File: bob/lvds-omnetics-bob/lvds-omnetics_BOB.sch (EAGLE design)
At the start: 31 parts, among them U1 SN65LVDS1, U2 SN65LVDS2, U3 SN65LVDS1, U4 SN65LVDS2, U5 SN65LVDS1, U6 SN65LVDS1

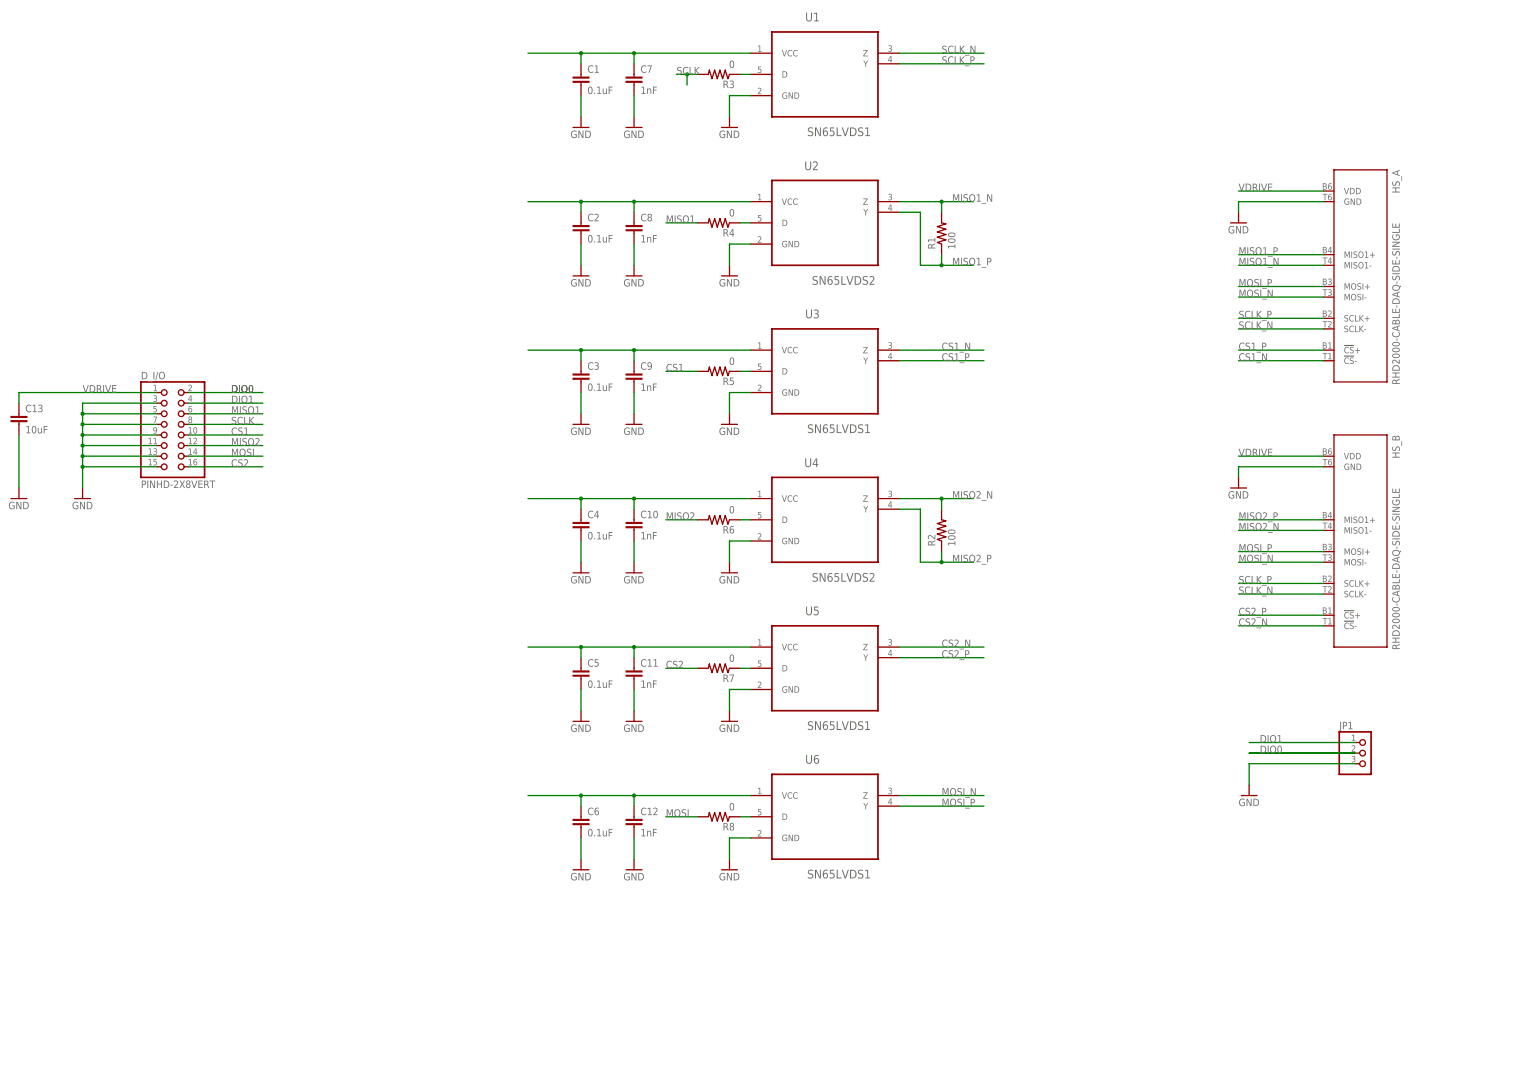
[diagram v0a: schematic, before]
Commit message: Fixed logo and made a part in the puggleboard library so that it is easy to add. Many minor changes to both boards. Should be just about ready to go.
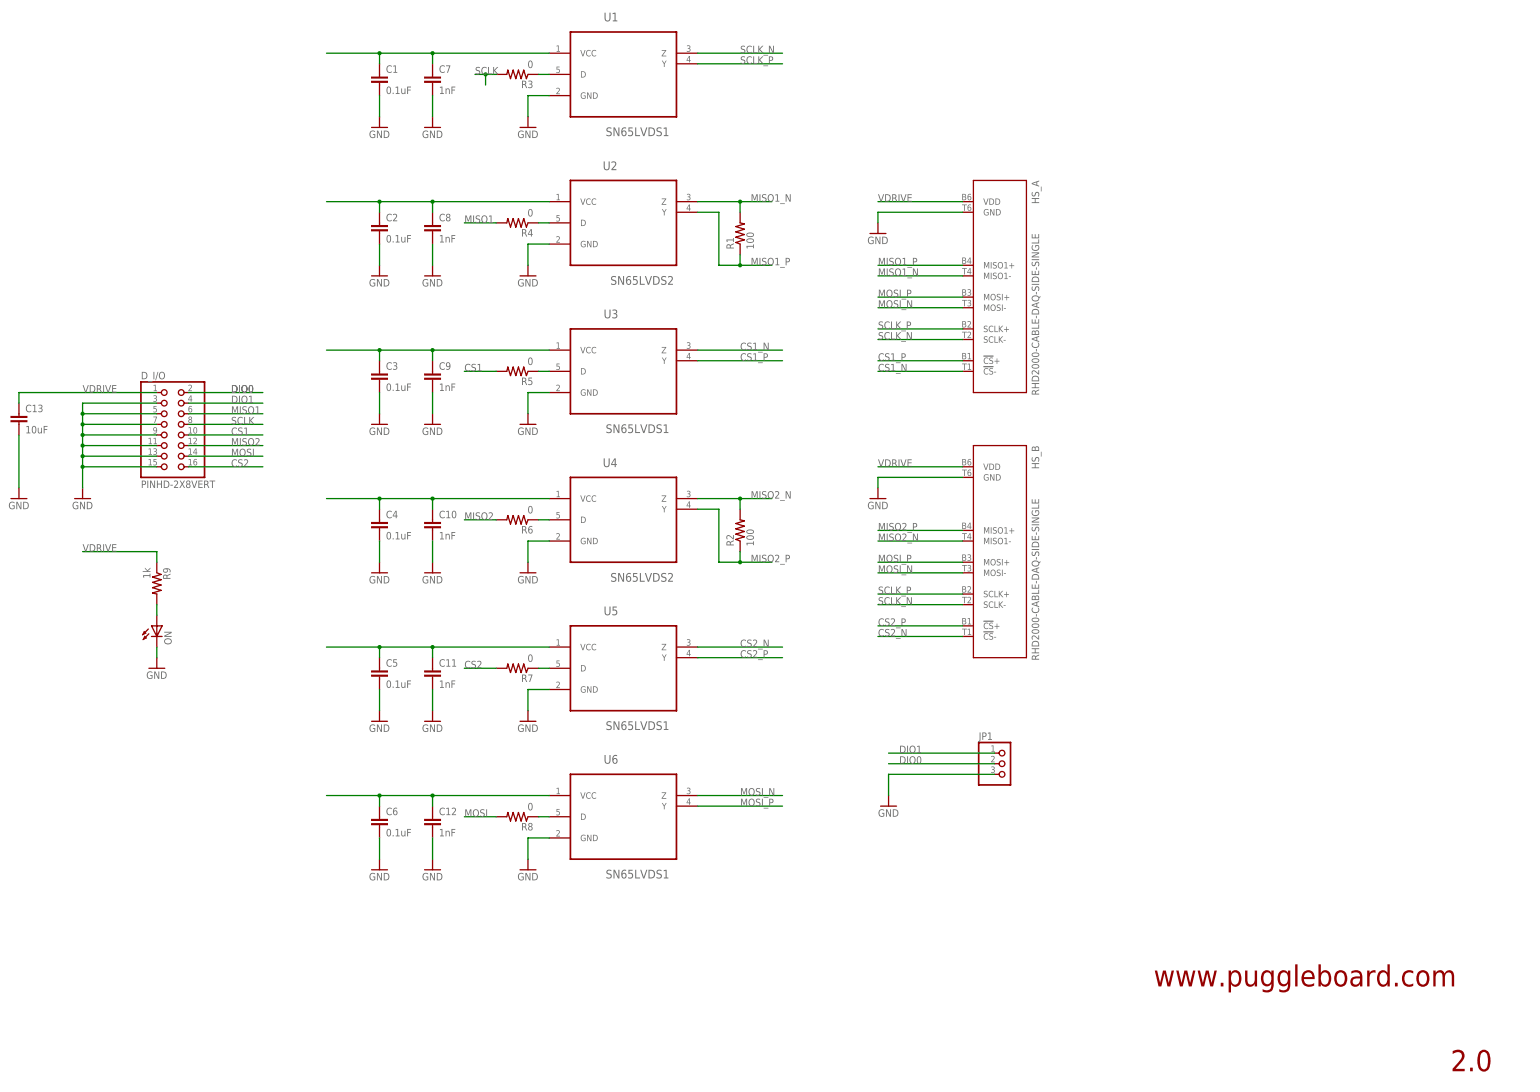
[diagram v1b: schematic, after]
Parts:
- added ON: LED-CHIP0805, puggleboard:LED-CHIP0805
- added R9: 1k, puggleboard:R_0603
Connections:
- new net N$9: ON.A, R9.2
- net GND: now also ON.C
- net VDRIVE: now also R9.1
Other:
- note added: "2.0"
- note added: "www.puggleboard.com"
- moved on the sheet: C1, C10, C11, C12, C2, C3, C4, C5, C6, C7, C8, C9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

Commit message: Many final changes to design before fabrication.
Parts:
- C1: value 0.1uF -> 10uF; device puggleboard:C_0603 -> puggleboard:C_0805
- C13: value 10uF -> 1nF; device puggleboard:C_0805 -> puggleboard:C_0603
- C7: value 1nF -> 0.1uF
- R1: value 100 -> 1k
- R2: value 100 -> 0
- R8: value 0 -> 100
- R9: value 1k -> 100
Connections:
- removed net VDRIVE: C1.1, C10.1, C11.1, C12.1, C13.1, C2.1, C3.1, C4.1, C5.1, C6.1, C7.1, C8.1, C9.1, D_I/O.1, HS_A.VDD, HS_B.VDD, R9.1, U1.VCC, U2.VCC, U3.VCC, U4.VCC, U5.VCC, U6.VCC
- new net VCC: C1.1, C10.1, C11.1, C12.1, C13.1, C2.1, C3.1, C4.1, C5.1, C6.1, C7.1, C8.1, C9.1, D_I/O.1, HS_A.VDD, HS_B.VDD, R1.1, U1.VCC, U2.VCC, U3.VCC, U4.VCC, U5.VCC, U6.VCC
- net CS1: now also R4.2; no longer R5.2
- net CS2: now also R6.2; no longer R7.2
- net MISO1: now also R3.2; no longer R4.2
- net MISO1_N: now also R8.2; no longer R1.2
- net MISO1_P: now also R8.1; no longer R1.1
- net MISO2: now also R5.2; no longer R6.2
- net MISO2_N: now also R9.2; no longer R2.2
- net MISO2_P: now also R9.1; no longer R2.1
- net MOSI: now also R7.2; no longer R8.2
- net N$2: now also R3.1; no longer R4.1
- net N$3: now also R4.1; no longer R5.1
- net N$4: now also R5.1; no longer R6.1
- net N$5: now also R6.1; no longer R7.1
- net N$6: now also R7.1; no longer R8.1
- net N$7: now also R2.1; no longer R3.1
- net N$9: now also R1.2; no longer R9.2
- net SCLK: now also R2.2; no longer R3.2
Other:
- note added: "VCC = VDRIVE = 3.3 VOLTS (FROM BEAGLEBONE SUPPLY)"
- moved on the sheet: C1, C10, C11, C12, C13, C2, C3, C4, C5, C6, C7, C8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
